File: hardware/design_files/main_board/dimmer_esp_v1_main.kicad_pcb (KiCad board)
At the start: 2 copper layers, 42 x 39.5 mm, 42 parts, among them J1 SM05B-SRSS-TB_LF__SN_, J3 Plug_1, J4 Conn_01x02, J5 Conn_01x02, J6 Conn_01x02, J7 Conn_01x04, SW2 Encoder Button, U1 Encoder: PES12-40S-N0024, U2 LDO: SPX3819M5-L-3-3, U3 ESP32-C6-MINI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

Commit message: Save as kicad 9.0.2, update libraries
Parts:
- D3: footprint SparkFun-LED:WS2812_5050-4Pin -> LED_SMD:LED_WS2812B_PLCC4_5.0x5.0mm_P3.2mm

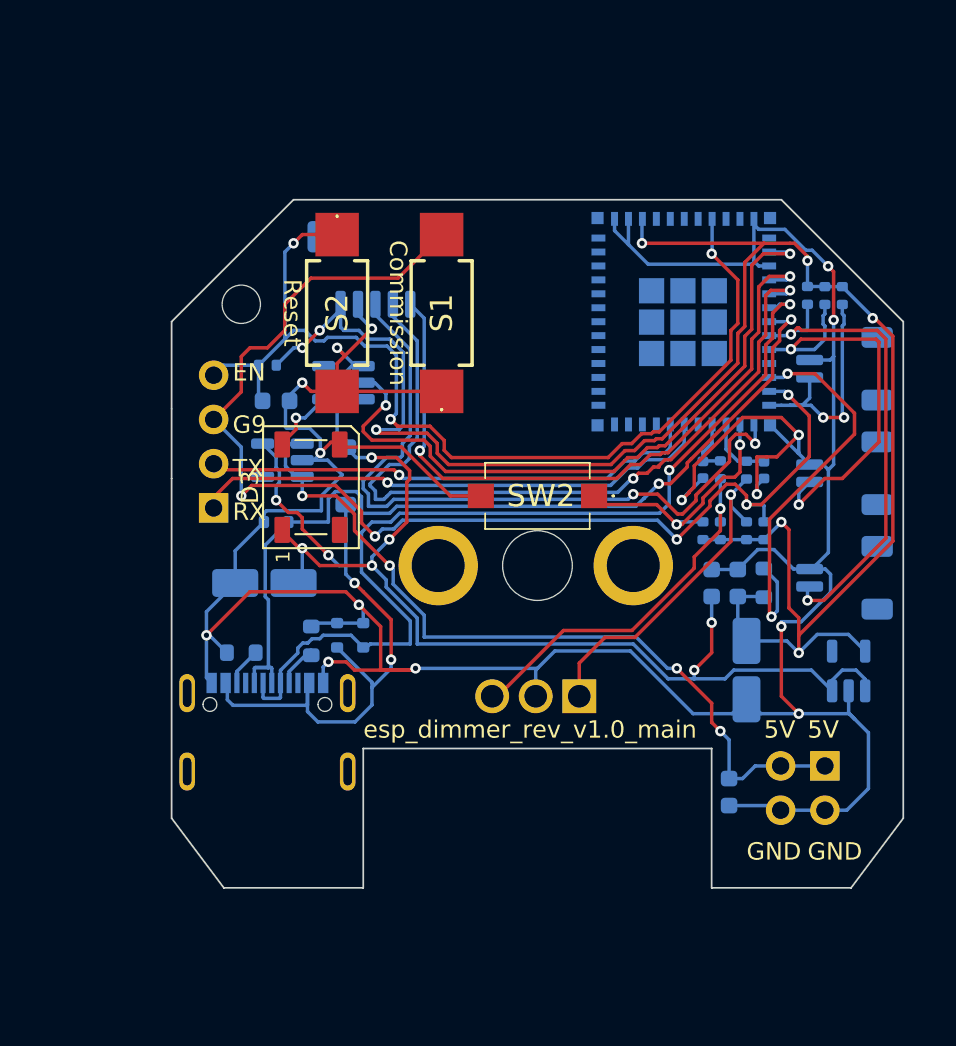
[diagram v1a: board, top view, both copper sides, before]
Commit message: Add components, version with relay, needs re-layout of tracks
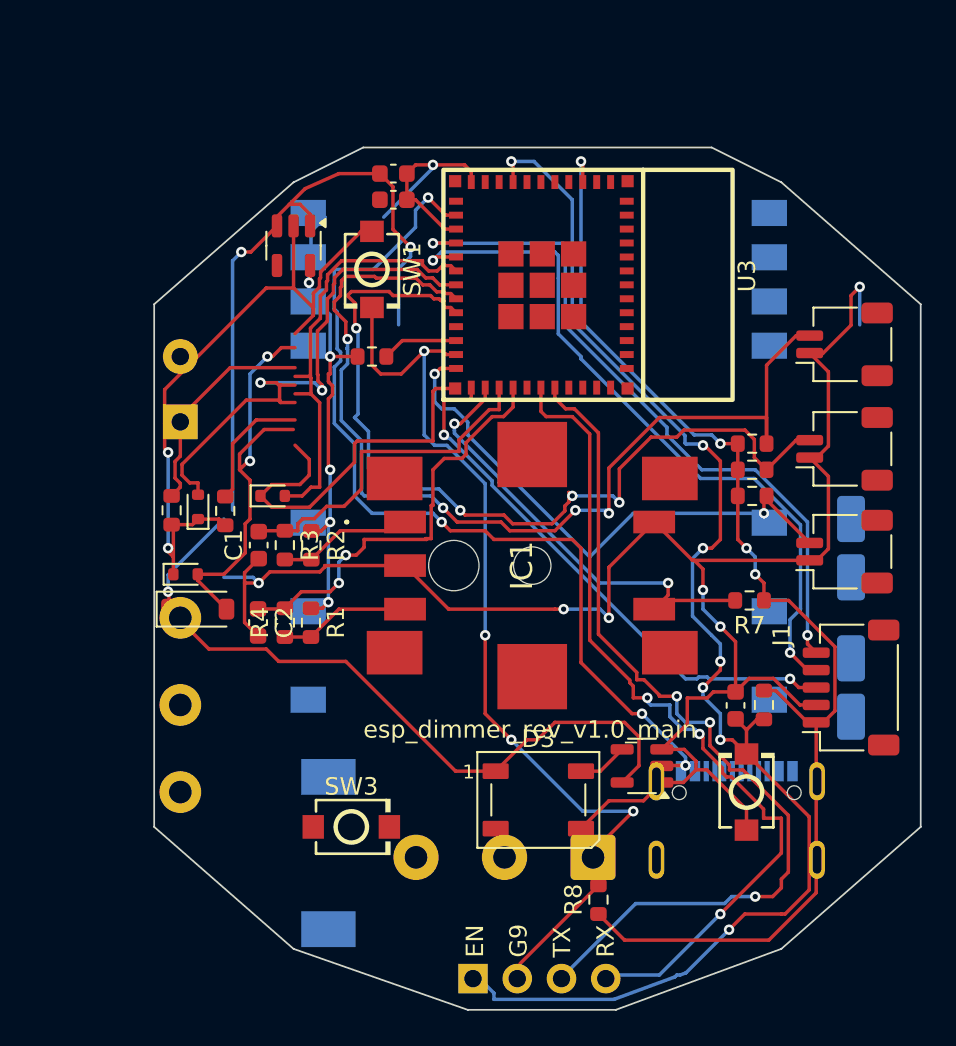
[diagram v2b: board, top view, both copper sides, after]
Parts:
- removed C8: 1u, Capacitor_SMD:C_0603_1608Metric
- removed H1: MountingHole, MountingHole:MountingHole_2.2mm_M2_DIN965
- removed J3: Plug_1, Connector_PinHeader_2.54mm:PinHeader_2x02_P2.54mm_Vertical
- removed S1, S2: Switch: PTS636_SM25F_SMTR_LFS, button_ck:PTS636_SM25F_SMTR_LFS
- removed U1: Encoder: PES12-40S-N0024, bourns_encoder:PES1240SN0024
- removed U6: LDO: SSP7603P50M5R, Package_TO_SOT_SMD:SOT-23-5
- added F1: Fuse 230V 500mA Slow, jlc_misc:0443.500DR, B.Cu at (155.5, 77.5)
- added IC1: PEC11S-929K-S0015, bourns_encoder:PEC11S929KS0015, F.Cu at (167.2, 61.0)
- added J8: Screw_Terminal_01x03, TerminalBlock_Phoenix:TerminalBlock_Phoenix_MKDS-1,5-3-5.08_1x03_P5.08mm_Horizontal, B.Cu at (170.7, 77.7)
- added K2: FINDER-34.51, Relay_THT:Relay_SPDT_Finder_34.51_Vertical, B.Cu at (147.0, 52.8)
- added PS2: IRM-02-5S, Converter_ACDC:Converter_ACDC_MeanWell_IRM-02-xx_SMD, B.Cu at (167.6, 54.7)
- added SW1: Commission, button_jlc:SW-SMD_L3.9-W3.0-P4.45, F.Cu at (158.0, 44.0)
- added SW3: Commission, button_jlc:SW-SMD_L3.9-W3.0-P4.45, F.Cu at (156.8, 76.0)
- C1, C2: footprint Capacitor_SMD:C_0402_1005Metric -> Capacitor_SMD:C_0603_1608Metric; moved to F.Cu
- C5, C6, C7, D1, D2, D4, D5, J1, J4, J5, J6, R12, R5, R6, U2, U3, U4: moved to F.Cu
- R1, R10, R11, R14, R2, R3, R4, R7, R8, R9: footprint Resistor_SMD:R_0402_1005Metric -> Resistor_SMD:R_0603_1608Metric; moved to F.Cu
- SW2: value Encoder Button -> Reset; footprint button_diptronics:TAEF25SVTR -> button_jlc:SW-SMD_L3.9-W3.0-P4.45
- moved U2 40.1 mm to (153.5, 42.6), turned to -90 degrees
- moved J1 36.3 mm to (185.5, 68.0), turned to 90 degrees
- moved R14 34.5 mm to (180.5, 69.0), turned to -90 degrees
- moved C3 34.2 mm to (185.5, 68.0), turned to 90 degrees
- moved C5 31.6 mm to (178.9, 69.0), turned to -90 degrees
- moved J7 30.8 mm to (163.8, 84.7), turned to -90 degrees
- moved C6 29.8 mm to (159.2, 38.5), turned to 180 degrees
- moved C7 29.6 mm to (159.2, 40.0), turned to 180 degrees
- moved C1 29.3 mm to (151.5, 59.8)
- moved U4 27.9 mm to (173.5, 72.5)
- moved USB1 27.4 mm to (178.9, 75.3)
- moved C2 27.0 mm to (151.5, 64.3)
- moved R3 26.8 mm to (153.0, 59.8)
- moved R4 26.5 mm to (153.0, 64.3)
- moved R12 26.0 mm to (158.0, 49.0), turned to 180 degrees
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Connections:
- SW2 pad 1: /D20 -> GND
- SW2 pad 2: GND -> /EN
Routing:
- net Net-(J3-Pin_1): track 45.2 -> 0.00 mm, vias 4 -> 0
- net GND: track 213.8 -> 178.2 mm, vias 15 -> 9
- net /D14: track 28.0 -> 58.3 mm, vias 2 -> 4
- net /D12: track 53.9 -> 25.3 mm, vias 2 -> 0
- net /D15: track 24.3 -> 50.9 mm, vias 2 -> 4
- net /UART_TXD: track 28.6 -> 51.4 mm, vias 1 -> 3
- net /EN: track 58.7 -> 80.0 mm, vias 3 -> 7
- net /D22: track 3.36 -> 24.3 mm, vias 0 -> 2
- net /D13: track 51.5 -> 31.7 mm
- net Net-(U3-IO8): track 22.9 -> 4.38 mm, vias 2 -> 0
- net /UART_RXD: track 30.3 -> 48.4 mm, vias 1 -> 3
- net /D18: track 13.7 -> 31.4 mm
- net /D09: track 70.5 -> 53.9 mm, vias 5 -> 4
- net /D21: track 3.90 -> 19.8 mm
- net /D01: track 39.7 -> 54.3 mm, vias 2 -> 4
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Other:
- board size 42 x 39.5 mm -> 44 x 49.5 mm
- board text removed: "5V"
- board text removed: "GND"

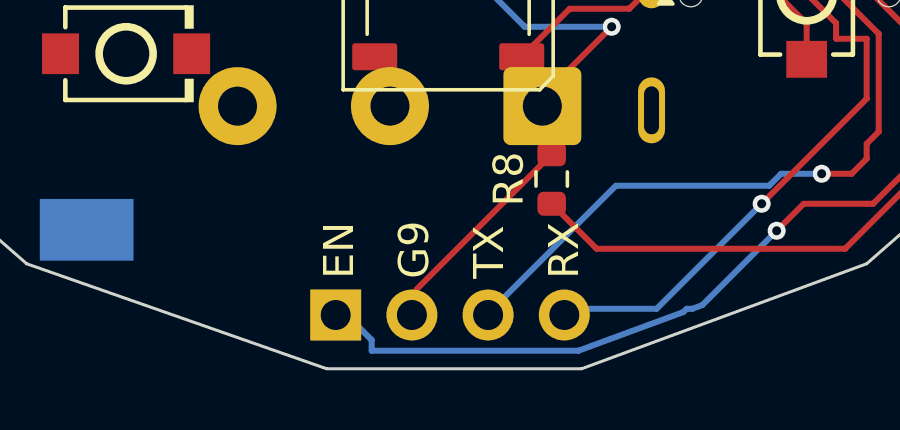
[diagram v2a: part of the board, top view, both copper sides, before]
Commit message: Adapt pin header
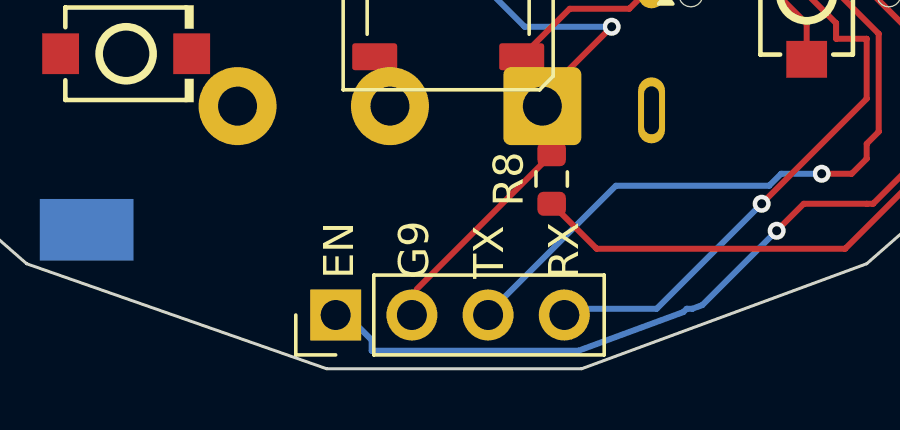
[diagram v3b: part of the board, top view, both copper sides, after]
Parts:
- J7: moved to F.Cu
- turned J7 to 90 degrees

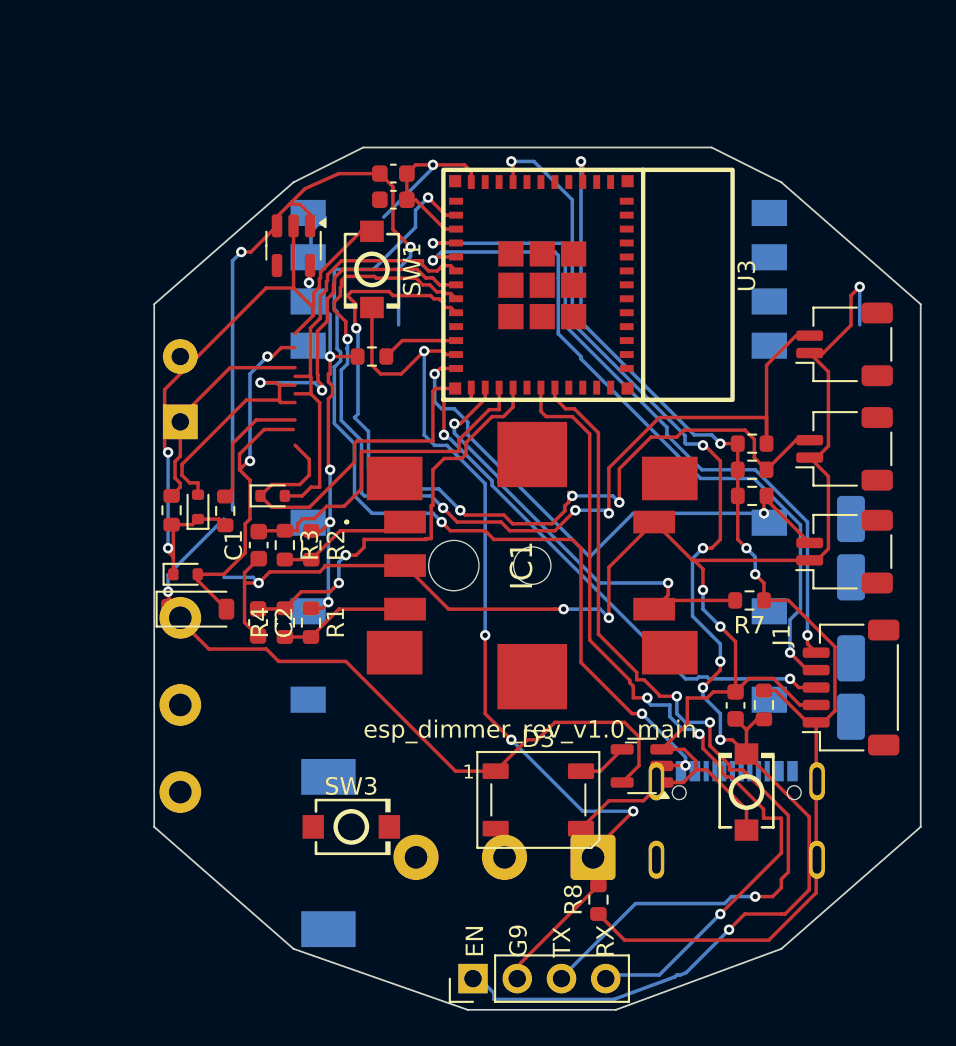
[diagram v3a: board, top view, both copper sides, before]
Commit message: Add toggle circuit, arrange components on PCB
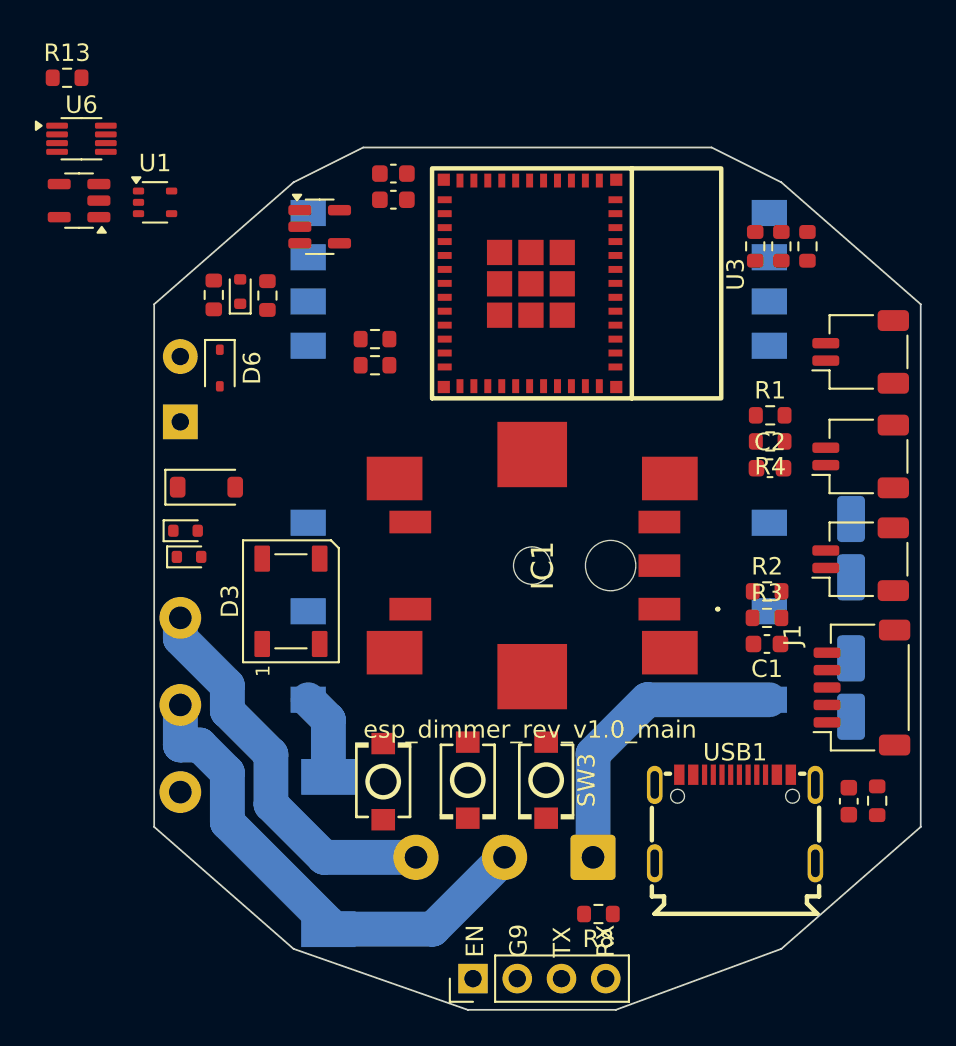
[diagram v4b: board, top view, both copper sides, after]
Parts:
- added D6: 1N4148WS, Diode_SMD:D_SOD-323, F.Cu at (149.3, 49.7)
- added R13: 10k, Resistor_SMD:R_0603_1608Metric, F.Cu at (140.5, 33.0)
- added U1: 74AHC1G14, Package_TO_SOT_SMD:SOT-353_SC-70-5, F.Cu at (145.6, 40.1)
- added U6: SN74LVC1G74, Package_SO:VSSOP-8_2.3x2mm_P0.5mm, F.Cu at (141.3, 36.5)
- SW3: value Commission -> Toggle
- USB1: moved to F.Cu
- moved U4 45.8 mm to (141.2, 40.0)
- moved C2 30.7 mm to (180.8, 55.4), turned to 180 degrees
- moved R4 29.7 mm to (180.9, 53.9), turned to 180 degrees
- moved C1 29.7 mm to (180.7, 65.5), turned to 180 degrees
- moved SW1 29.4 mm to (158.6, 73.4), turned to 90 degrees
- moved R1 28.9 mm to (180.9, 52.4), turned to 0 degrees
- moved R3 28.0 mm to (180.7, 64.0), turned to 0 degrees
- moved R2 26.3 mm to (180.7, 62.5), turned to 0 degrees
- moved R7 25.4 mm to (158.2, 49.5), turned to 0 degrees
- moved D3 18.2 mm to (153.3, 63.0), turned to 90 degrees
- moved SW2 16.0 mm to (163.5, 73.3), turned to -90 degrees
- moved R11 14.3 mm to (180.0, 42.7), turned to -90 degrees
- moved R10 12.9 mm to (181.5, 42.7), turned to -90 degrees
- moved R5 12.6 mm to (148.9, 45.5)
- moved R6 12.6 mm to (152.0, 45.5)
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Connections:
- J8 pad 1: /HV2 -> /HV1
- J8 pad 2: /HV1 -> /HV2
- K2 pad 11: /HV3 -> /HV2
- K2 pad A2: Net-(K2-PadA2) -> Net-(D6-K)
- SW3 pad 1: Net-(K2-PadA2) -> GND
- SW3 pad 2: +5V -> Net-(R13-Pad2)
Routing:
- net GND: track 178.2 -> 0.00 mm, vias 9 -> 0
- net +3.3V: track 97.4 -> 0.00 mm, vias 9 -> 0
- net /EN: track 80.0 -> 0.00 mm, vias 7 -> 0
- net +5V: track 78.1 -> 0.00 mm, vias 3 -> 0
- net /D14: track 58.3 -> 0.00 mm, vias 4 -> 0
- net /D01: track 54.3 -> 0.00 mm, vias 4 -> 0
- net /D09: track 53.9 -> 0.00 mm, vias 4 -> 0
- net /UART_TXD: track 51.4 -> 0.00 mm, vias 3 -> 0
- net /D15: track 50.9 -> 0.00 mm, vias 4 -> 0
- net /UART_RXD: track 48.4 -> 0.00 mm, vias 3 -> 0
- net /D07: track 40.9 -> 0.00 mm, vias 2 -> 0
- net /D06: track 40.1 -> 0.00 mm, vias 2 -> 0
- net /D19: track 31.9 -> 0.00 mm, vias 2 -> 0
- net /D13: track 31.7 -> 0.00 mm, vias 2 -> 0
- net /D18: track 31.4 -> 0.00 mm, vias 2 -> 0
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
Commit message: Wired everything up
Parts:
- moved D1 43.4 mm to (188.0, 74.0), turned to -90 degrees
- moved D5 41.8 mm to (186.0, 75.0), turned to -90 degrees
- moved R5 39.0 mm to (180.0, 69.0), turned to -90 degrees
- moved R6 37.7 mm to (181.5, 69.0), turned to 90 degrees
- moved R13 24.2 mm to (158.2, 49.5)
- moved D2 20.7 mm to (159.3, 43.5)
- moved U4 19.1 mm to (152.6, 55.4), turned to -90 degrees
- moved U6 17.0 mm to (154.8, 46.9), turned to -90 degrees
- moved C5 13.5 mm to (174.6, 82.7)
- moved R14 13.5 mm to (176.3, 82.7)
- moved U1 13.4 mm to (153.3, 51.0), turned to 90 degrees
- moved R1 7.44 mm to (180.7, 59.8), turned to 180 degrees
- moved R7 6.41 mm to (155.5, 55.3), turned to -90 degrees
- moved R4 4.44 mm to (180.7, 58.3), turned to 0 degrees
- moved R2 3.04 mm to (180.7, 65.5), turned to 180 degrees
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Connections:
- J1 pad 4: /D07 -> Net-(J1-Pad4)
- J1 pad 5: /D06 -> Net-(J1-Pad5)
- K2 pad 11: /HV2 -> /HV4
- K2 pad 12: /HV4 -> /HV3
- K2 pad A1: GND -> Net-(D6-K)
- K2 pad A2: Net-(D6-K) -> GND
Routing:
- net GND: track 0.00 -> 242.7 mm, vias 0 -> 14
- net +3.3V: track 0.00 -> 125.8 mm, vias 0 -> 8
- net +5V: track 0.00 -> 84.5 mm, vias 0 -> 4
- net /D13: track 0.00 -> 60.2 mm, vias 0 -> 7
- net /D09: track 0.00 -> 52.1 mm
- net /D12: track 0.00 -> 51.4 mm, vias 0 -> 6
- net /D18: track 0.00 -> 47.0 mm, vias 0 -> 4
- net /D15: track 0.00 -> 40.8 mm, vias 0 -> 4
- net /UART_RXD: track 0.00 -> 38.8 mm, vias 0 -> 2
- net /D07: track 0.00 -> 38.5 mm, vias 0 -> 2
- net /D06: track 0.00 -> 38.3 mm, vias 0 -> 2
- net /D19: track 0.00 -> 38.2 mm, vias 0 -> 2
- net /UART_TXD: track 0.00 -> 37.3 mm, vias 0 -> 2
- net /D14: track 0.00 -> 34.5 mm, vias 0 -> 4
- net Net-(R13-Pad2): track 0.00 -> 33.6 mm, vias 0 -> 2
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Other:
- board text added: "esp_dimmer_v2.0"
- board text removed: "esp_dimmer_rev_v1.0_main"
